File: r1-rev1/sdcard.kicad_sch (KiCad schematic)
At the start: 6 parts, among them J3 TF-115

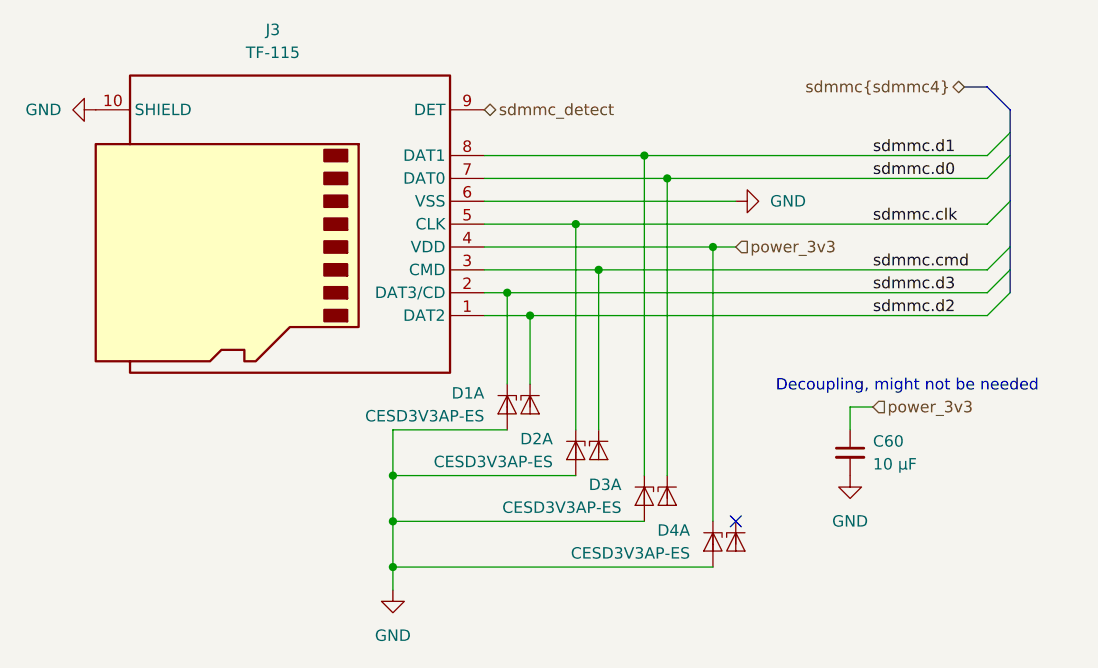
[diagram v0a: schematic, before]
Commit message: R1-Rev1: document errata for SDMMC bus ESD diodes
ESD diodes on the SDMMC bus have too high a capacitance and
cause errors particularly during high-speed operation (50MHz).
Mark as DNP on the schematic.

See Github issue: #27
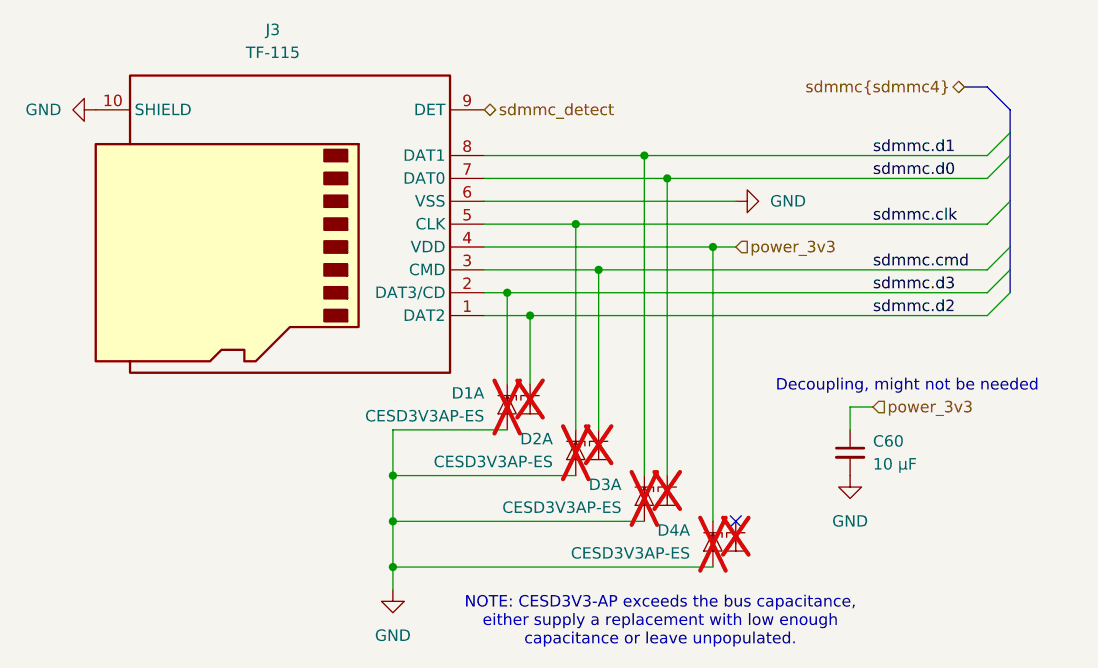
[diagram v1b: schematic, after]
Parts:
- D1, D2, D3, D4: now not fitted; now left out of the parts list
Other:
- note added: "NOTE: CESD3V3-AP exceeds the bus capacitance, either supply a replacement with low enough capacitance or leave unpopulated."
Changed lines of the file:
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@@
 		(comment 3 "NOT RECOMMENDED FOR MANUFACTURE")
+	)
+	(text "NOTE: CESD3V3-AP exceeds the bus capacitance,\neither supply a replacement with low enough\ncapacitance or leave unpopulated."
+		(exclude_from_sim no)
+		(at 161.798 140.716 0)
+		(effects
+			(font
+				(size 1.27 1.27)
+			)
+		)
 	)
 	(text "Decoupling, might not be needed"
@@
 		(unit 2)
 		(exclude_from_sim no)
-		(in_bom yes)
+		(in_bom no)
 		(on_board yes)
-		(dnp no)
+		(dnp yes)
 		(fields_autoplaced yes)
 		(property "Reference" "D4"
@@
 		(unit 1)
 		(exclude_from_sim no)
-		(in_bom yes)
+		(in_bom no)
 		(on_board yes)
-		(dnp no)
+		(dnp yes)
 		(property "Reference" "D3"
 			(at 157.48 125.4759 90)
@@
 		(unit 2)
 		(exclude_from_sim no)
-		(in_bom yes)
+		(in_bom no)
 		(on_board yes)
-		(dnp no)
+		(dnp yes)
 		(fields_autoplaced yes)
 		(property "Reference" "D3"
@@
 		(unit 2)
 		(exclude_from_sim no)
-		(in_bom yes)
+		(in_bom no)
 		(on_board yes)
-		(dnp no)
+		(dnp yes)
 		(fields_autoplaced yes)
 		(property "Reference" "D2"
@@
 		(unit 1)
 		(exclude_from_sim no)
-		(in_bom yes)
+		(in_bom no)
 		(on_board yes)
-		(dnp no)
+		(dnp yes)
 		(property "Reference" "D2"
 			(at 149.86 120.3959 90)
@@
 		(unit 1)
 		(exclude_from_sim no)
-		(in_bom yes)
+		(in_bom no)
 		(on_board yes)
-		(dnp no)
+		(dnp yes)
 		(property "Reference" "D1"
 			(at 142.24 115.3159 90)
@@
 		(unit 1)
 		(exclude_from_sim no)
-		(in_bom yes)
+		(in_bom no)
 		(on_board yes)
-		(dnp no)
+		(dnp yes)
 		(property "Reference" "D4"
 			(at 165.1 130.5559 90)
@@
 		(unit 2)
 		(exclude_from_sim no)
-		(in_bom yes)
+		(in_bom no)
 		(on_board yes)
-		(dnp no)
+		(dnp yes)
 		(fields_autoplaced yes)
 		(property "Reference" "D1"
